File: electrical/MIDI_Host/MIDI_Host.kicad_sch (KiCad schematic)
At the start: 27 parts, among them CN1 USB-CON-AF-LCP-Offset, J2 (NF), SW2 TC-1109DE-C-G, U13 LN1134A332MR-G, U15 SESRV05-4

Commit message: SUKU sync
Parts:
- C15: value (none) -> 100n
- D10, D8, D9: value (none) -> UI_WS2812C-2020; footprint (none) -> suku_basics:UI_WS2812C-2020_LIGHTPIPE
- J1: value (none) -> MC-107DM
- R12: value (none) -> 5k1
- R9: value (none) -> 1k
- SW1: value (none) -> ST-0-102-C03-N003-RS
- U11, U12: value (none) -> BL1551B
- U14: value (none) -> SESRV05-4
- U4: value (none) -> ESP32-S3-WROOM-1U
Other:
- moved on the sheet: C15, C16, D10, D8, D9, J2, R10, R11, R12, R16, R18, R19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

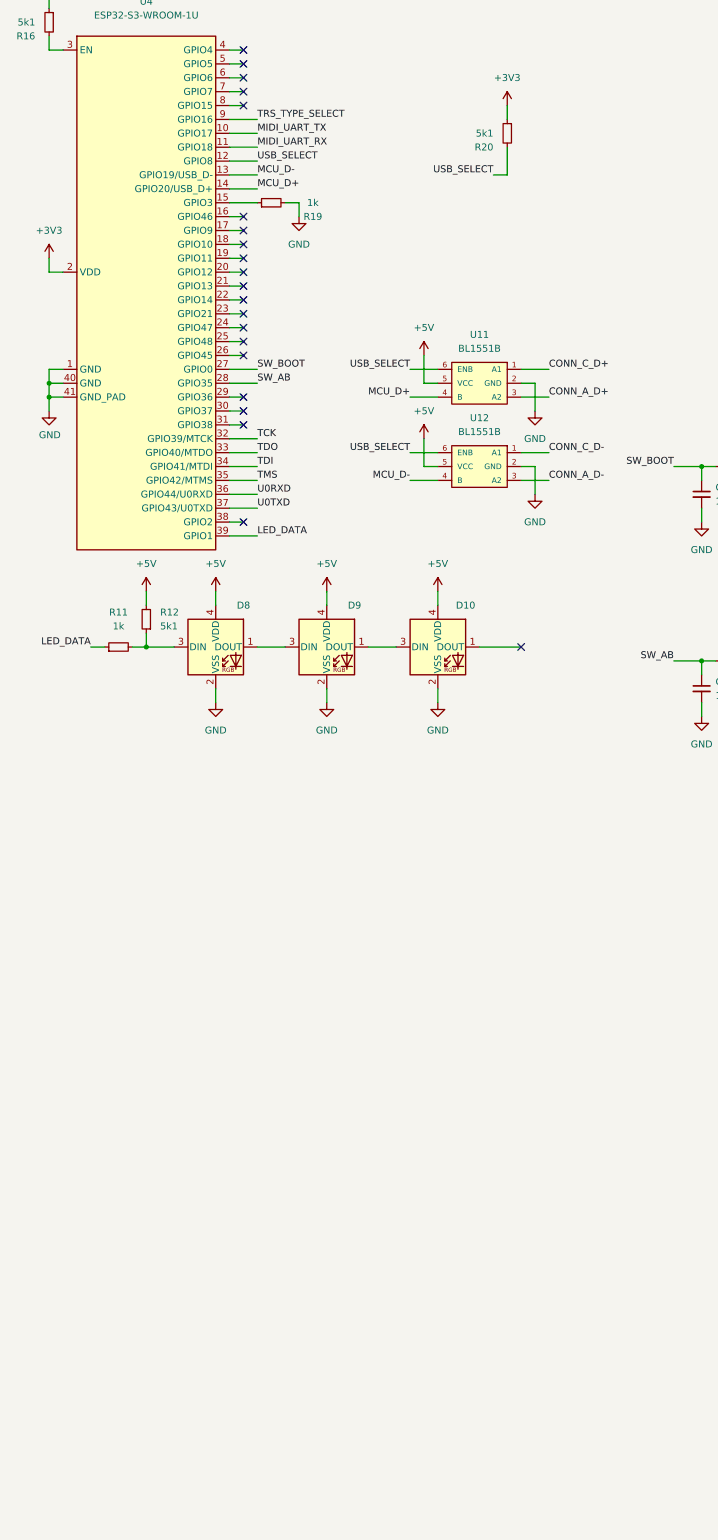
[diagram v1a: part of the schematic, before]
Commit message: SUKU successful enumeration and MIDI out test
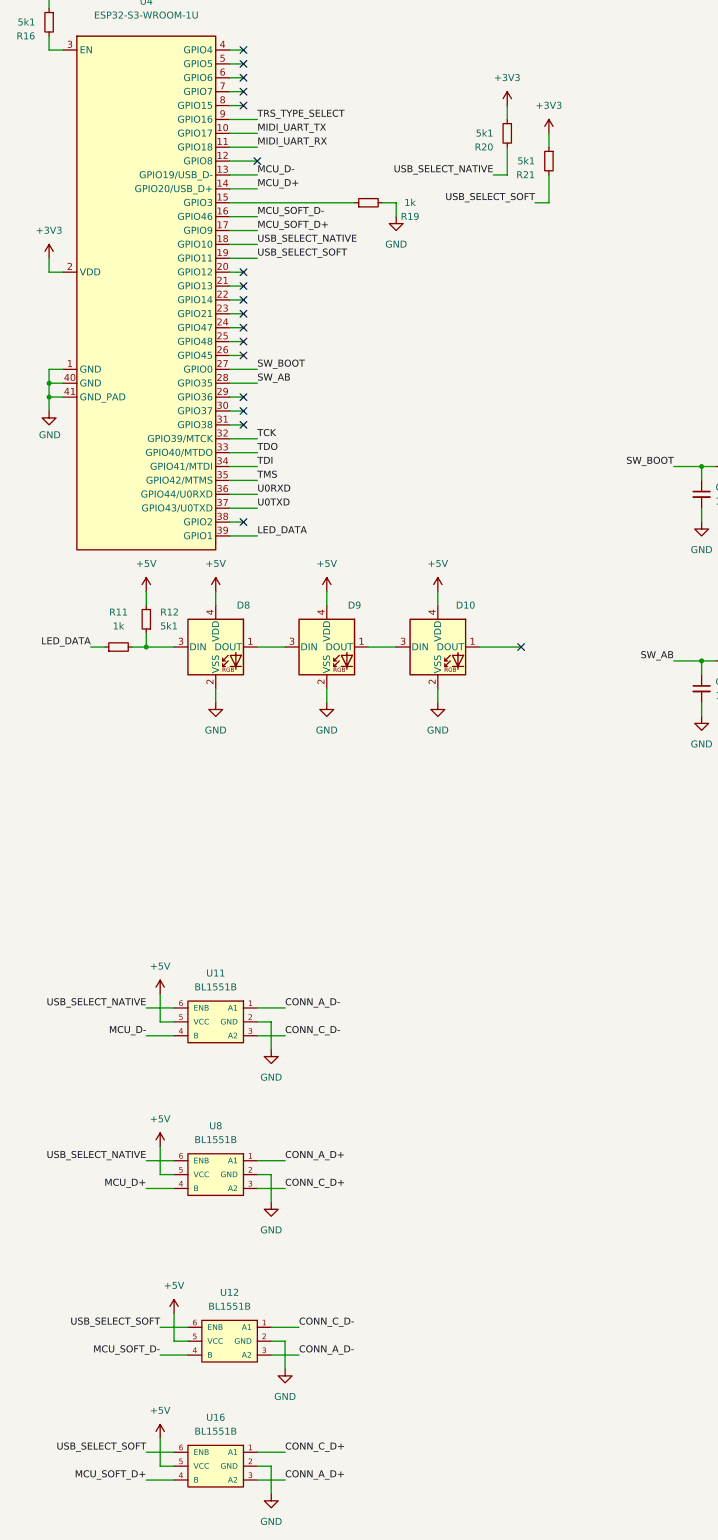
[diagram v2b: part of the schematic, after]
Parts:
- added R21: 5k1, suku_basics:RES_0805, symbol suku_basics:RES
- added U16, U8: BL1551B, suku_basics:SOT-363_SC-70-6, symbol suku_basics:BL1551B
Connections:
- net +3V3: now also R21.1
- net +5V: now also U16.5 (VCC), U8.5 (VCC)
- net CONN_A_D+: now also U16.3 (A2), U8.1 (A1); no longer U11.3 (A2)
- net CONN_A_D-: now also U11.1 (A1)
- net CONN_C_D+: now also U16.1 (A1), U8.3 (A2); no longer U11.1 (A1)
- net CONN_C_D-: now also U11.3 (A2)
- net GND: now also U16.2 (GND), U8.2 (GND)
- net MCU_D+: now also U8.4 (B); no longer U11.4 (B)
- net MCU_D-: now also U11.4 (B); no longer U12.4 (B)
- net MCU_SOFT_D-: now reaches U4.16 (GPIO46)
- net MCU_SOFT_D-: now also U12.4 (B)
- net MCU_SOFT_D+: now reaches U4.17 (GPIO9)
- net MCU_SOFT_D+: now also U16.4 (B)
- net USB_SELECT_NATIVE: now reaches U4.18 (GPIO10)
- net USB_SELECT_NATIVE: now also R20.2, U11.6 (ENB), U8.6 (ENB)
- net USB_SELECT_SOFT: now reaches U4.19 (GPIO11)
- net USB_SELECT_SOFT: now also U12.6 (ENB), R21.2, U16.6 (ENB)
- removed net USB_SELECT: R20.2, U11.6 (ENB), U12.6 (ENB), U4.12 (GPIO8)
- no-connect marks 30 -> 27
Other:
- moved on the sheet: R19, U11, U12

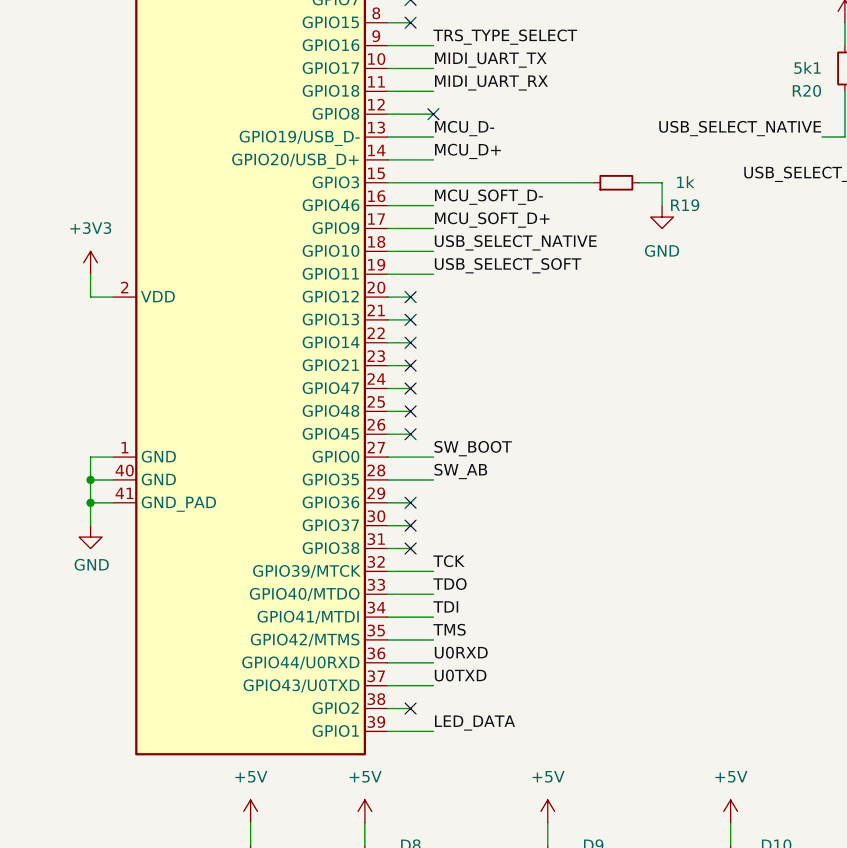
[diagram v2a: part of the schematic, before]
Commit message: SUKU Midi host initial design + layout done
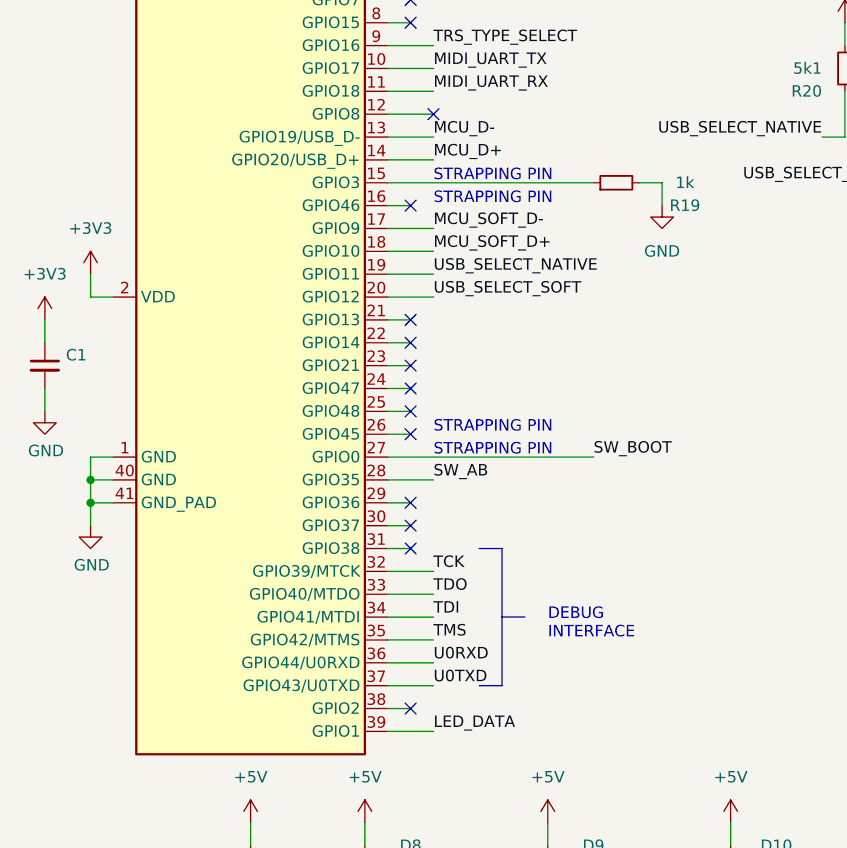
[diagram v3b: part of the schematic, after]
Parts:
- added C1: (no value), suku_basics:CAP_0805, symbol suku_basics:CAP
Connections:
- net +3V3: now also C1.1
- net GND: now also C1.2
- net MCU_SOFT_D+: now also U4.18 (GPIO10); no longer U4.17 (GPIO9)
- net MCU_SOFT_D-: now also U4.17 (GPIO9); no longer U4.16 (GPIO46)
- net USB_SELECT_NATIVE: now also U4.19 (GPIO11); no longer U4.18 (GPIO10)
- net USB_SELECT_SOFT: now also U4.20 (GPIO12); no longer U4.19 (GPIO11)
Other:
- note added: "DEBUG INTERFACE"
- note added: "STRAPPING PIN"

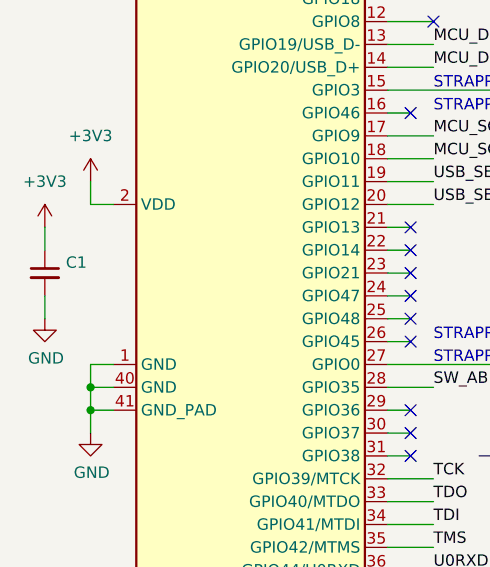
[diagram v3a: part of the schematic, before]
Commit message: SUKU dangling wire in schematic removed
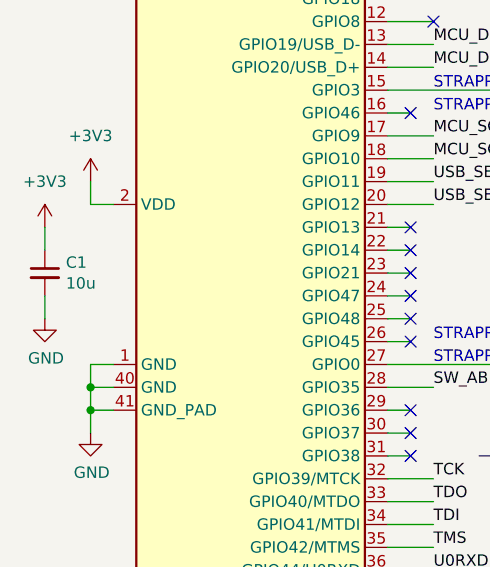
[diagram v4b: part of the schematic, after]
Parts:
- C1: value (none) -> 10u
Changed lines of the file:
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@@
       (effects (font (size 1.27 1.27)) (justify left))
     )
-    (property "Value" "" (id 1) (at 22.6568 117.983 0)
+    (property "Value" "10u" (id 1) (at 22.6568 117.983 0)
       (effects (font (size 1.27 1.27)) (justify left))
     )

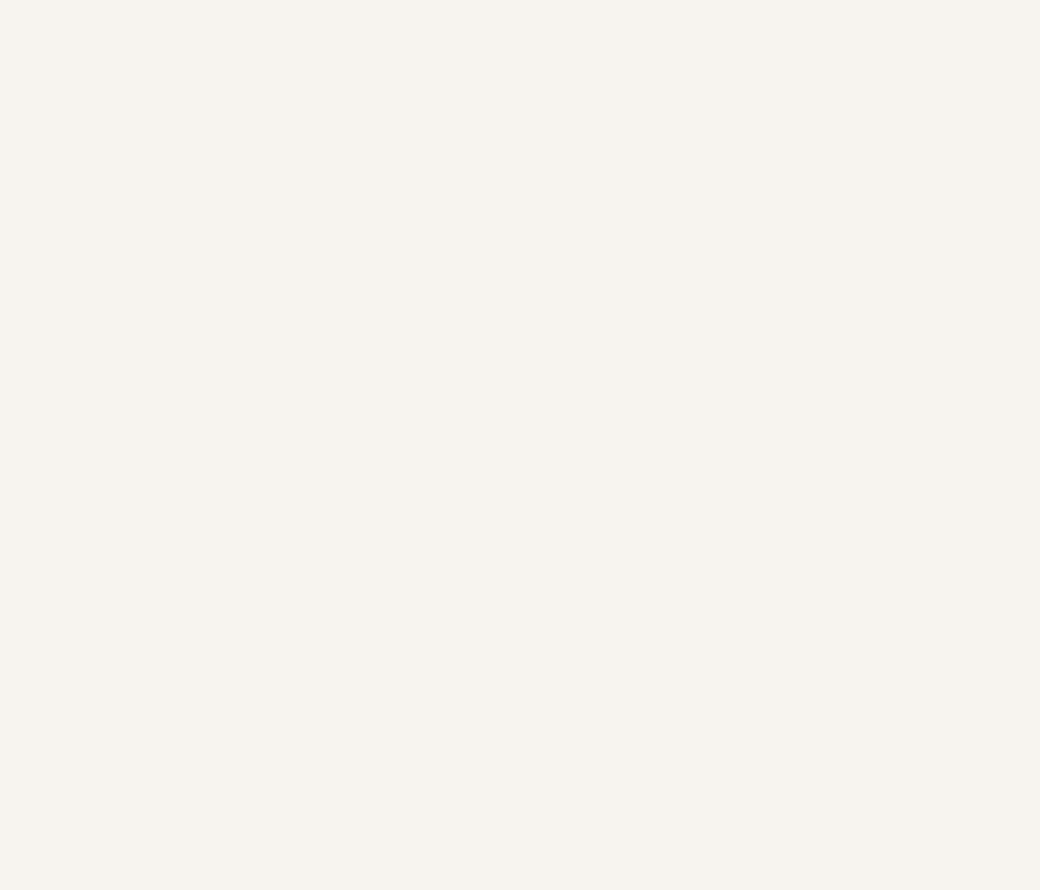
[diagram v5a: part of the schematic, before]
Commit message: SUKU mechanical exports added
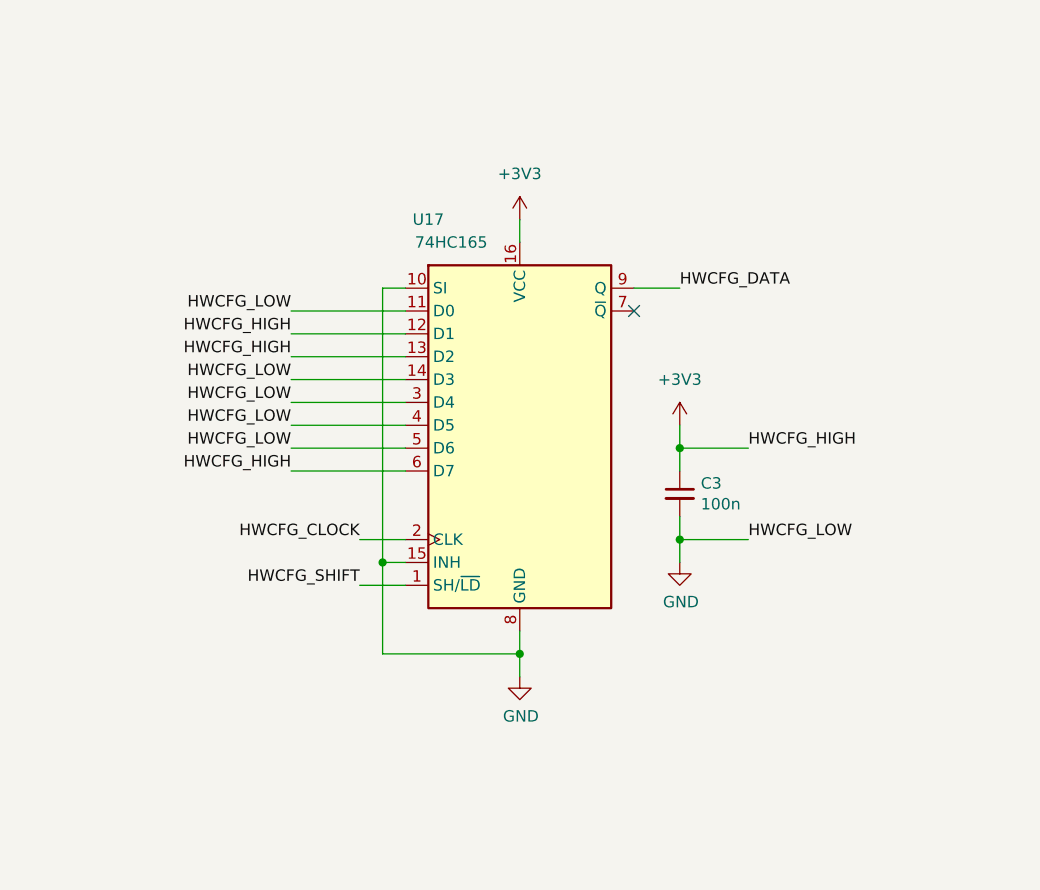
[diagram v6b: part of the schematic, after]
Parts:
- added C3: 100n, suku_basics:CAP_0805, symbol suku_basics:CAP
- added U17: 74HC165, suku_basics:SOIC-16_74HC165, symbol suku_basics:74HC165
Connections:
- net +3V3: now also C3.1, U17.12 (D1), U17.13 (D2), U17.16 (VCC), U17.6 (D7)
- net GND: now also C3.2, U17.10 (SI), U17.11 (D0), U17.14 (D3), U17.15 (INH), U17.3 (D4), U17.4 (D5), U17.5 (D6), U17.8 (GND)
- new net HWCFG_CLOCK: U17.2 (CLK)
- new net HWCFG_DATA: U17.9 (Q)
- new net HWCFG_SHIFT: U17.1 (SH/~{LD})
- no-connect marks 27 -> 28

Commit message: SUKU pcb revision done
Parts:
- removed C17: 1u, suku_basics:CAP_0805, symbol suku_basics:CAP
- removed U13: LN1134A332MR-G, suku_basics:SOT-23-5, symbol suku_basics:U_REGULATOR_SOT23-5
- added TP1, TP14, TP15, TP2: (no value), symbol Connector:TestPoint_Alt
- added TP10: D+, TestPoint:TestPoint_THTPad_D1.0mm_Drill0.5mm, symbol Connector:TestPoint_Alt
- added TP13, TP16: G, TestPoint:TestPoint_THTPad_1.0x1.0mm_Drill0.5mm, symbol Connector:TestPoint_Alt
- added TP3, TP4, TP5, TP6, TP7: (no value), TestPoint:TestPoint_THTPad_D1.0mm_Drill0.5mm, symbol Connector:TestPoint_Alt
- added TP8: (no value), TestPoint:TestPoint_THTPad_1.0x1.0mm_Drill0.5mm, symbol Connector:TestPoint_Alt
- added TP9: D-, TestPoint:TestPoint_THTPad_D1.0mm_Drill0.5mm, symbol Connector:TestPoint_Alt
- C15: value 100n -> 100n (N.F.)
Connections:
- net +3V3: no longer R20.1, R21.1
- net +5V: now also TP7.1
- net CONN_A_D+: now also TP10.1
- net CONN_A_D-: now also TP9.1
- net CONN_C_D+: now also TP6.1
- net CONN_C_D-: now also TP5.1
- net GND: now also R20.1, R21.1, TP13.1, TP16.1, TP2.1, TP8.1
- net HWCFG_CLOCK: now also U4.24 (GPIO47)
- net HWCFG_DATA: now also U4.22 (GPIO14)
- net HWCFG_SHIFT: now also U4.23 (GPIO21)
- net MIDI_UART_RX: now also TP15.1
- net MIDI_UART_TX: now also TP14.1
- net SW_BOOT: now also U4.29 (GPIO36), TP4.1; no longer U4.27 (GPIO0)
- net TRS_TX_AB_SELECT: now reaches U4.8 (GPIO15)
- net at D10.1 (DOUT): now also TP3.1
- net TRS_TYPE_SELECT renamed TRS_RX_AB_SELECT
- new net: TP1.1, U4.27 (GPIO0)
- no-connect marks 28 -> 22
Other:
- sheet MIDI Frontened ports: added RX, RX_AB_SELECT, TX, TX_AB_SELECT; removed INVERTED_UART_MIDI_RX, INVERTED_UART_MIDI_TX, TRS_TYPE_A
- moved on the sheet: R20, R21
